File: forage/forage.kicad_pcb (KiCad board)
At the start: 2 copper layers, 308 x 79.4 mm, 69 parts, among them J1 Conn_01x04_MountingPin, Q1 AO3400A, U1 STM32G431RBTx, U2 XC6206P322MR

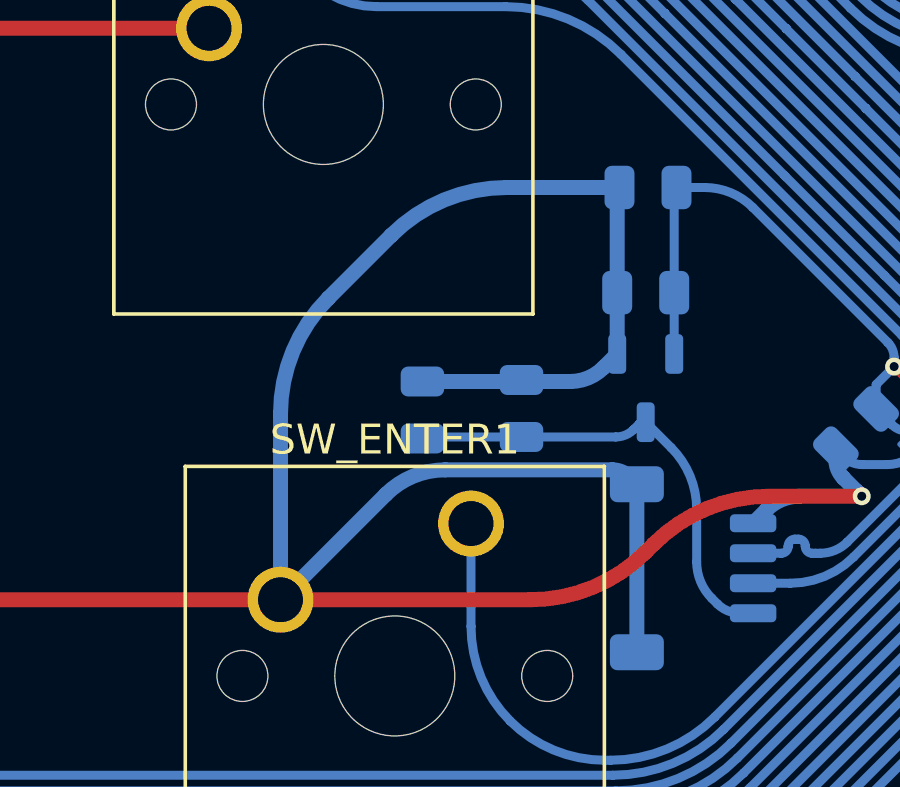
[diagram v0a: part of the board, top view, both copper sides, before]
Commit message: round a trace a little more
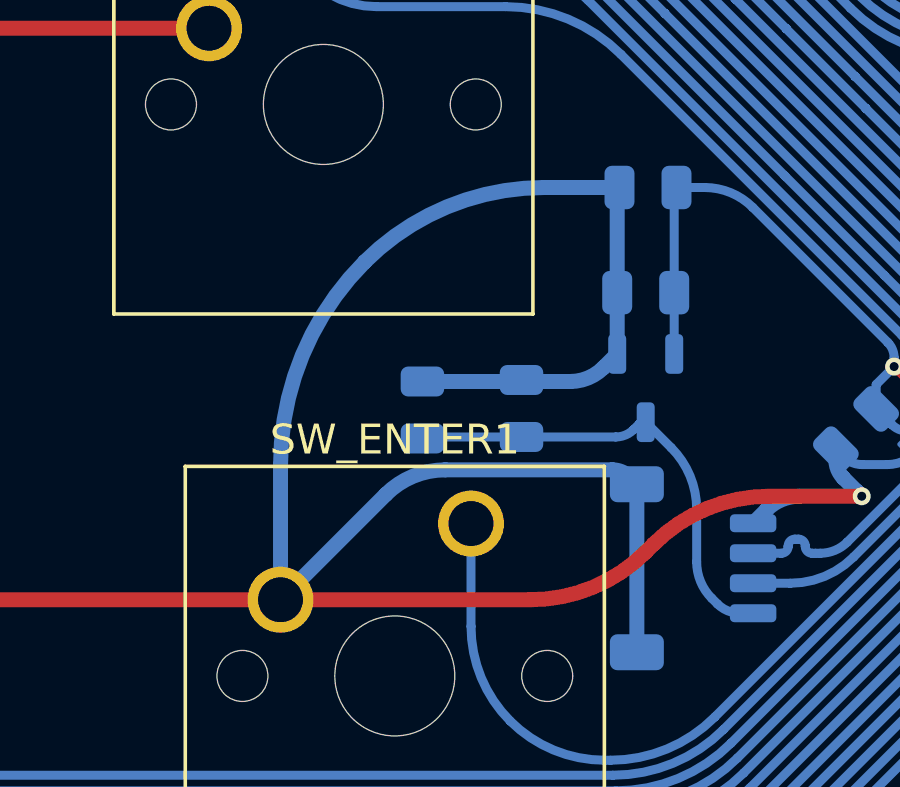
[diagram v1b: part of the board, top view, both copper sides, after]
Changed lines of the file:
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@@
 	)
 	(segment
-		(start 281.14625 143.657713)
+		(start 281.14625 145.37349)
 		(end 281.14625 149.86)
 		(width 0.5)
@@
 	)
 	(segment
-		(start 288.685363 136.1186)
+		(start 289.935896 136.1186)
 		(end 292.445401 136.1186)
 		(width 0.5)
@@
 		(start 318.428449 140.907849)
 		(end 319.4812 141.9606)
-		(width 0.5)
-		(layer "B.Cu")
-		(net 1)
-	)
-	(segment
-		(start 282.740042 139.809956)
-		(end 284.837607 137.712392)
 		(width 0.5)
 		(layer "B.Cu")
@@
 	)
 	(arc
-		(start 288.685363 136.1186)
-		(mid 286.602972 136.532813)
-		(end 284.837607 137.712392)
+		(start 289.935896 136.1186)
+		(mid 286.698163 136.762625)
+		(end 283.953346 138.596653)
 		(width 0.5)
 		(layer "B.Cu")
@@
 	)
 	(arc
-		(start 282.740042 139.809956)
-		(mid 281.560463 141.575322)
-		(end 281.14625 143.657713)
-		(width 0.5)
-		(layer "B.Cu")
+		(start 283.953346 138.596653)
+		(mid 281.875774 141.705926)
+		(end 281.14625 145.37349)
+		(width 0.5)
+		(layer "B.Cu")

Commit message: prepare a text area for attribution
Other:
- board text added: "forage version 2.0 by cn, girlypop.no"
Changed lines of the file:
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@@
 		(layer "Edge.Cuts")
+	)
+	(gr_text "forage version 2.0 by cn, girlypop.no"
+		(at 357.715 105.354 0)
+		(layer "B.SilkS")
+		(effects
+			(font
+				(size 1.5 1.5)
+				(thickness 0.3)
+				(bold yes)
+			)
+			(justify left bottom mirror)
+		)
 	)
 	(segment

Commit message: update silkscreen stuff
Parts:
- added G***: LOGO, LOGO, B.Cu at (206.7, 142.9)
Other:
- board text added: "forage version 2.0 by cn, girlypop.no; artwork by dwerple, twitch.tv/dwerple"
- board text removed: "forage version 2.0 by cn, girlypop.no"

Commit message: correct xc6206 thingy
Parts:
- U2: value XC6206P322MR -> XC6206P332MR
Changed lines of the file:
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@@
 			)
 		)
-		(property "Value" "XC6206P322MR"
+		(property "Value" "XC6206P332MR"
 			(at 0 -2.4 90)
 			(layer "B.Fab")

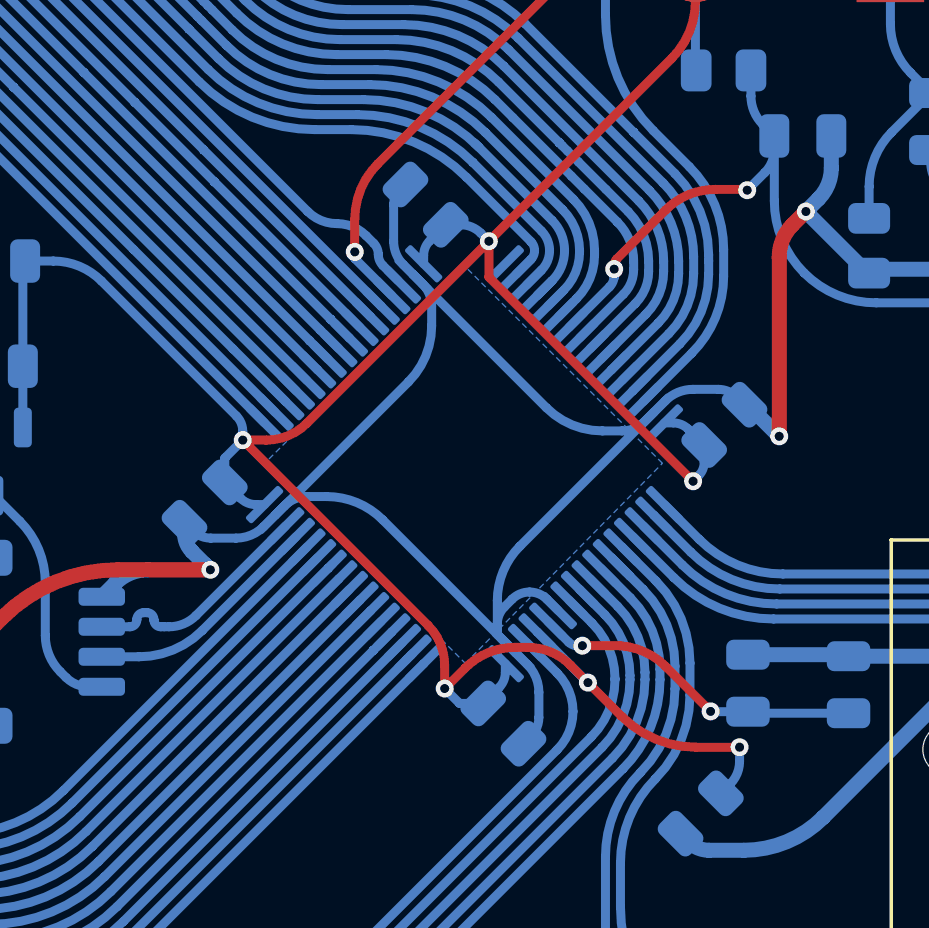
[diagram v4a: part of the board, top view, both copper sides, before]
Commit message: fix some pesky drc errors, make vbat trace follow 3.3v on the front side
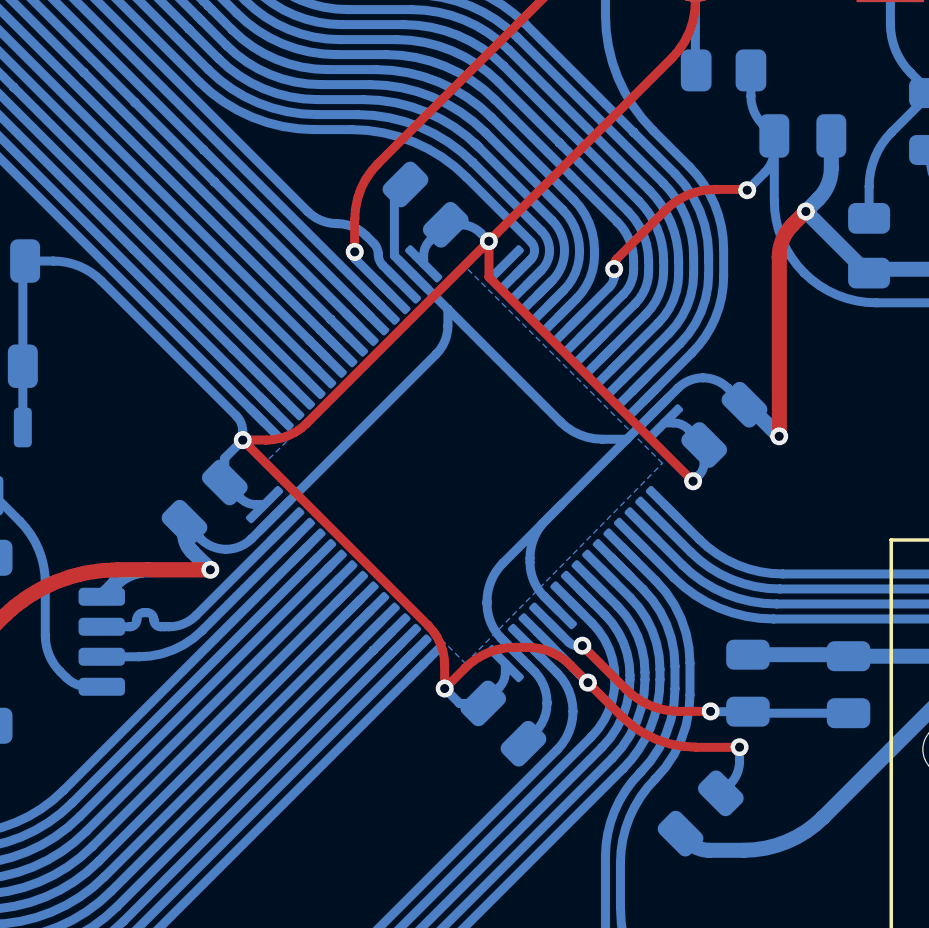
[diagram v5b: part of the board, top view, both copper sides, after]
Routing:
- net GND: track 1261.7 -> 1251.6 mm

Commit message: connect vbat to the 3.3v net
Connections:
- U1 pad 1: unconnected-(U1-VBAT-Pad1) -> +3.3V
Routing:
- net +3.3V: track 91.9 -> 95.3 mm
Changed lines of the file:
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@@
 	(net 56 "Y")
 	(net 57 "Z")
-	(net 58 "unconnected-(U1-VBAT-Pad1)")
 	(footprint "Button_Switch_Keyboard:SW_Cherry_MX_1.00u_PCB"
 		(layer "F.Cu")
@@
 			(layers "B.Cu" "B.Paste" "B.Mask")
 			(roundrect_rratio 0.25)
-			(net 58 "unconnected-(U1-VBAT-Pad1)")
+			(net 3 "+3.3V")
 			(pinfunction "VBAT")
 			(pintype "power_in")
@@
 	)
 	(segment
+		(start 308.242383 136.796383)
+		(end 307.665958 136.219958)
+		(width 0.3)
+		(layer "B.Cu")
+		(net 3)
+	)
+	(segment
 		(start 294.2692 136.194799)
 		(end 294.345399 136.1186)
@@
 	)
 	(segment
+		(start 307.643169 136.210519)
+		(end 307.629819 136.210519)
+		(width 0.3)
+		(layer "B.Cu")
+		(net 3)
+	)
+	(segment
 		(start 307.828599 135.449502)
 		(end 308.367351 134.910751)
@@
 	)
 	(segment
+		(start 309.766314 136.796383)
+		(end 310.352178 136.210519)
+		(width 0.3)
+		(layer "B.Cu")
+		(net 3)
+	)
+	(segment
 		(start 308.827249 150.864649)
 		(end 308.3306 150.368)
@@
 	)
 	(arc
+		(start 308.242383 136.796383)
+		(mid 308.591976 137.029973)
+		(end 309.004349 137.112)
+		(width 0.3)
+		(layer "B.Cu")
+		(net 3)
+	)
+	(arc
 		(start 316.450877 141.721579)
 		(mid 316.220751 141.567814)
@@
 	)
 	(arc
+		(start 310.352181 136.210519)
+		(mid 310.352179 136.210519)
+		(end 310.352178 136.210519)
+		(width 0.3)
+		(layer "B.Cu")
+		(net 3)
+	)
+	(arc
+		(start 309.766314 136.796383)
+		(mid 309.416721 137.029973)
+		(end 309.004349 137.112)
+		(width 0.3)
+		(layer "B.Cu")
+		(net 3)
+	)
+	(arc
 		(start 318.1604 152.797213)
 		(mid 318.079359 153.204631)
@@
 		(width 0.3)
 		(layer "B.Cu")
+		(net 3)
+	)
+	(arc
+		(start 307.665958 136.219958)
+		(mid 307.655502 136.212972)
+		(end 307.643169 136.210519)
+		(width 0.3)
+		(layer "B.Cu")

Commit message: recommended schmeccomended??? ok
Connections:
- U1 pad 1: +3.3V -> unconnected-(U1-VBAT-Pad1)
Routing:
- net +3.3V: track 95.3 -> 91.9 mm
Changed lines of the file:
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@@
 	(net 56 "Y")
 	(net 57 "Z")
+	(net 58 "unconnected-(U1-VBAT-Pad1)")
 	(footprint "Button_Switch_Keyboard:SW_Cherry_MX_1.00u_PCB"
 		(layer "F.Cu")
@@
 			(layers "B.Cu" "B.Paste" "B.Mask")
 			(roundrect_rratio 0.25)
-			(net 3 "+3.3V")
+			(net 58 "unconnected-(U1-VBAT-Pad1)")
 			(pinfunction "VBAT")
 			(pintype "power_in")
@@
 	)
 	(segment
-		(start 308.242383 136.796383)
-		(end 307.665958 136.219958)
-		(width 0.3)
-		(layer "B.Cu")
-		(net 3)
-	)
-	(segment
 		(start 294.2692 136.194799)
 		(end 294.345399 136.1186)
@@
 	)
 	(segment
-		(start 307.643169 136.210519)
-		(end 307.629819 136.210519)
-		(width 0.3)
-		(layer "B.Cu")
-		(net 3)
-	)
-	(segment
 		(start 307.828599 135.449502)
 		(end 308.367351 134.910751)
@@
 	)
 	(segment
-		(start 309.766314 136.796383)
-		(end 310.352178 136.210519)
-		(width 0.3)
-		(layer "B.Cu")
-		(net 3)
-	)
-	(segment
 		(start 308.827249 150.864649)
 		(end 308.3306 150.368)
@@
 	)
 	(arc
-		(start 308.242383 136.796383)
-		(mid 308.591976 137.029973)
-		(end 309.004349 137.112)
-		(width 0.3)
-		(layer "B.Cu")
-		(net 3)
-	)
-	(arc
 		(start 316.450877 141.721579)
 		(mid 316.220751 141.567814)
@@
 	)
 	(arc
-		(start 310.352181 136.210519)
-		(mid 310.352179 136.210519)
-		(end 310.352178 136.210519)
-		(width 0.3)
-		(layer "B.Cu")
-		(net 3)
-	)
-	(arc
-		(start 309.766314 136.796383)
-		(mid 309.416721 137.029973)
-		(end 309.004349 137.112)
-		(width 0.3)
-		(layer "B.Cu")
-		(net 3)
-	)
-	(arc
 		(start 318.1604 152.797213)
 		(mid 318.079359 153.204631)
@@
 		(width 0.3)
 		(layer "B.Cu")
-		(net 3)
-	)
-	(arc
-		(start 307.665958 136.219958)
-		(mid 307.655502 136.212972)
-		(end 307.643169 136.210519)
-		(width 0.3)
-		(layer "B.Cu")

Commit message: wip: start work on moving the cluster 6 subunits to the right
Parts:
- moved SW_DELETE1 4.76 mm to (337.5, 109.2)
- moved SW_DOWN1 4.76 mm to (337.5, 166.4)
- moved SW_INSERT1 4.76 mm to (318.5, 109.2)
- moved SW_LEFT1 4.76 mm to (318.5, 166.4)
- moved SW_PRTSC1 4.76 mm to (356.6, 109.2)
- moved SW_RIGHT1 4.76 mm to (356.6, 166.4)
- moved SW_UP1 4.76 mm to (337.5, 147.3)
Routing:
- net PRTSC: track 62.0 -> 0.00 mm
- net DELETE: track 53.1 -> 0.00 mm
- net RIGHT: track 45.2 -> 0.00 mm
- net DOWN: track 36.1 -> 0.00 mm
- net INSERT: track 33.7 -> 0.00 mm
- net GND: track 1251.6 -> 1224.3 mm
- net LEFT: track 22.5 -> 0.87 mm
- net UP: track 18.7 -> 0.00 mm
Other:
- board size 308 x 79.4 mm -> 312.7 x 79.4 mm
